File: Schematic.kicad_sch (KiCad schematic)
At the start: 51 parts, among them IC601 AZV3002S-13, J101 KLDX-0202-B, J102 EBWA-02-B, J103 EBWA-02-B, J104 KLDX-0202-B, Q201 MCU18P10Y-TP, Q501 BC846, Q502 MCU18P10Y-TP, U401 LM4040DBZ-5

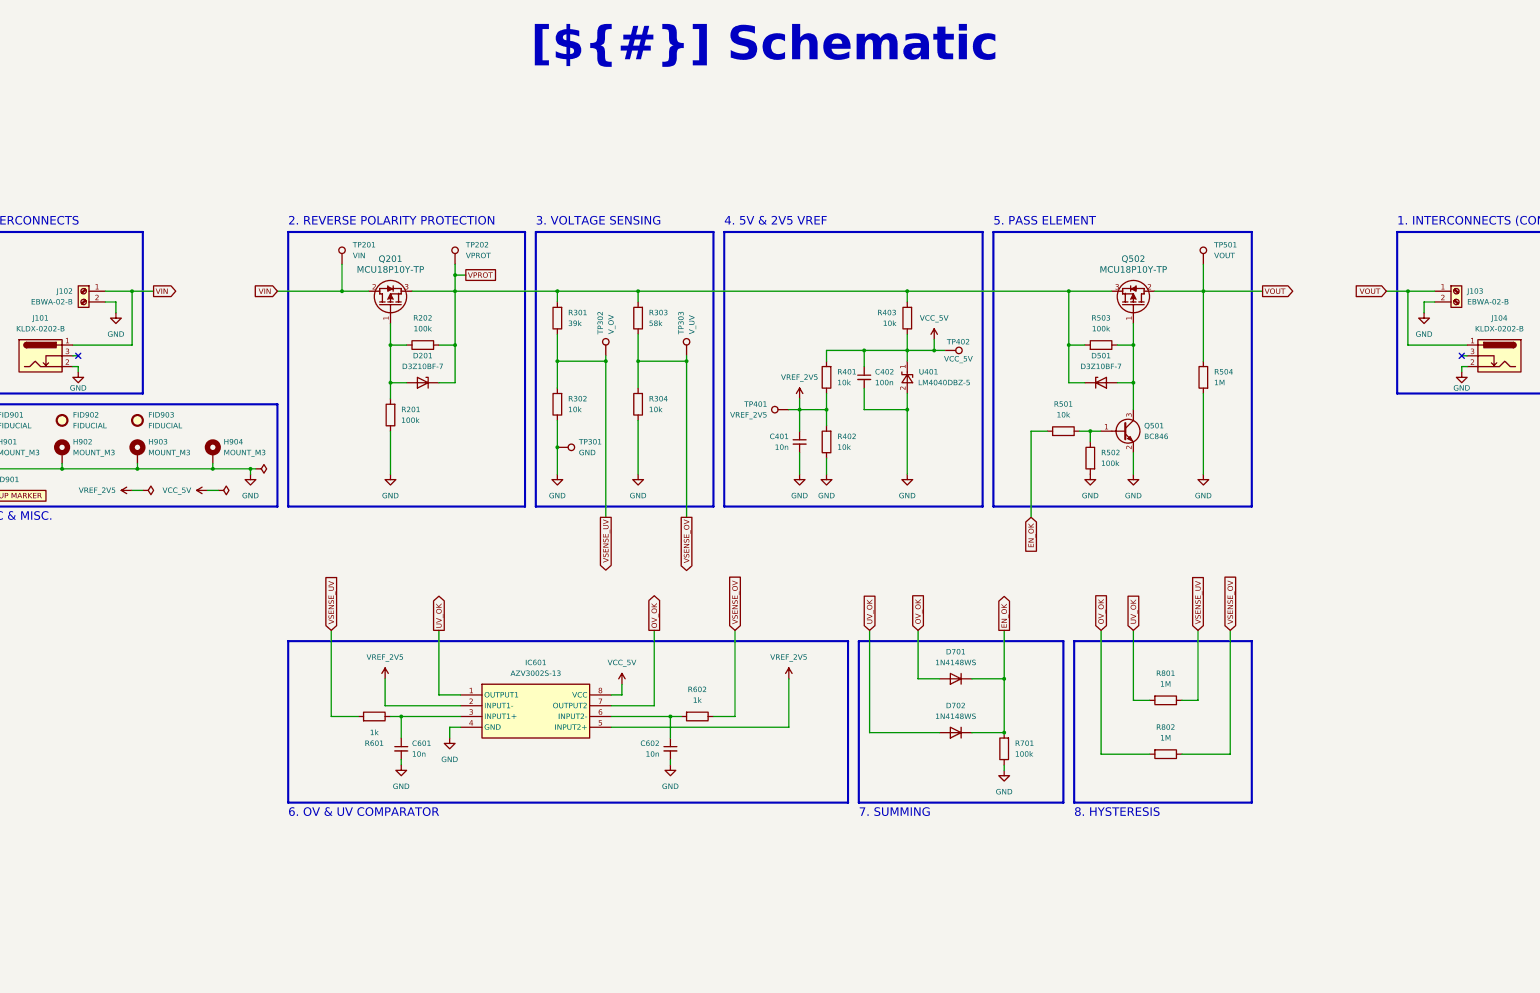
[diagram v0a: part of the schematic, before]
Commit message: fix: fix properties of actives with MPN
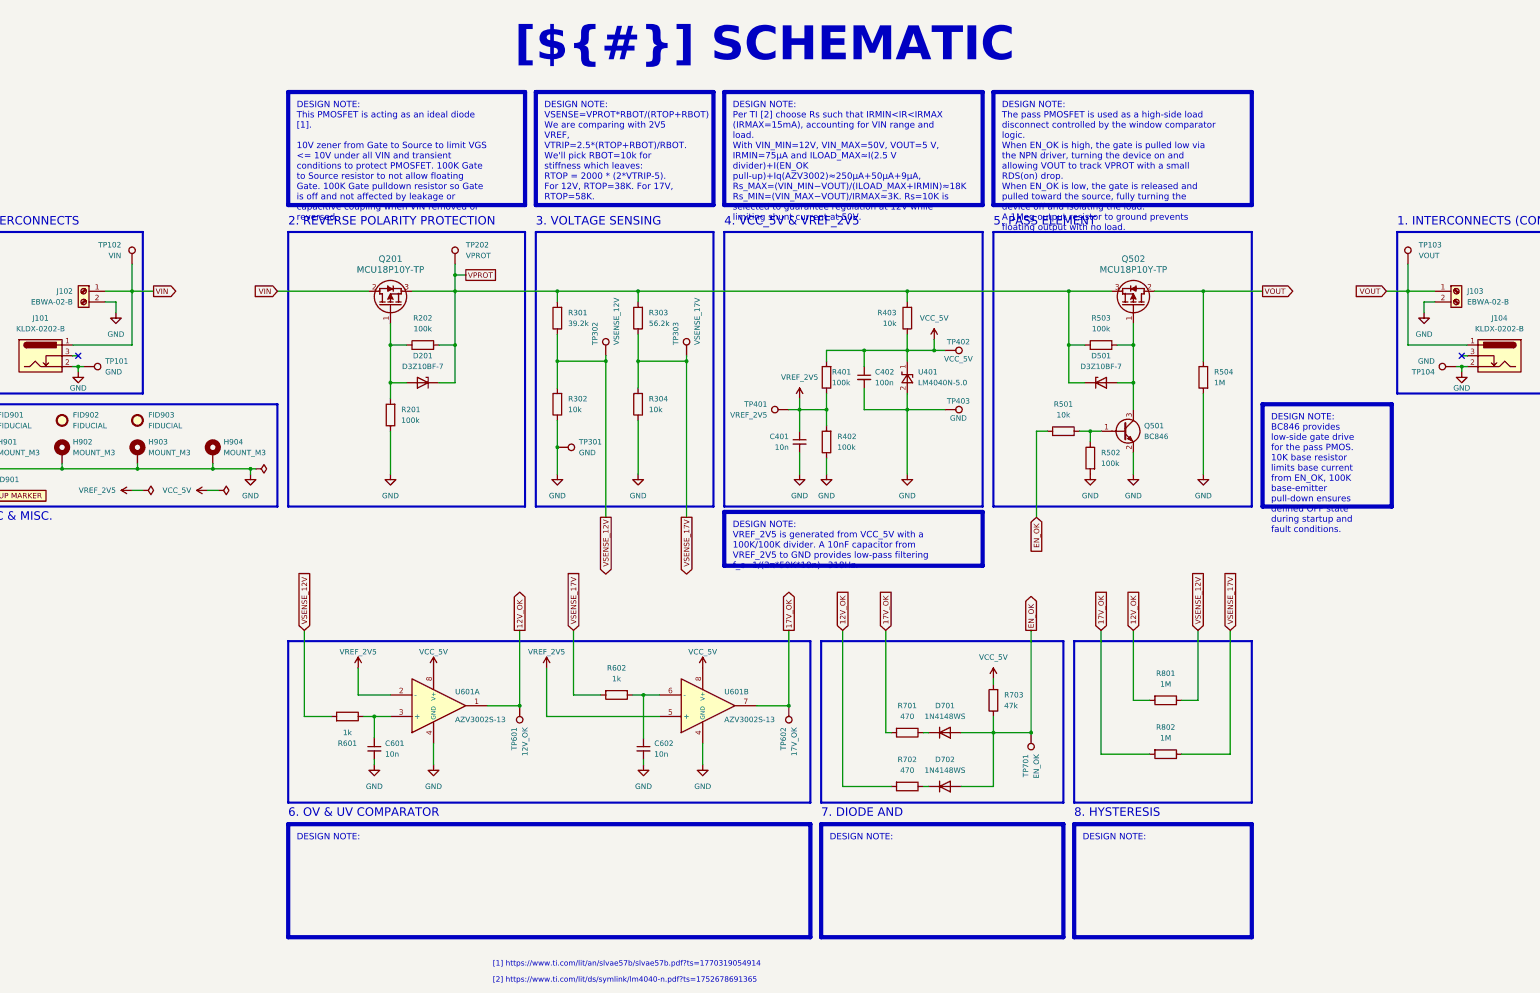
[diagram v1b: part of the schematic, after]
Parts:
- removed IC601: AZV3002S-13, Package_SO:Diodes_SO-8EP, symbol AZV3002S-13:AZV3002S-13
- added R701, R702: 470, Resistor_SMD:R_1206_3216Metric_Pad1.30x1.75mm_HandSolder, symbol Device:R
- added TP101, TP104, TP403: GND, TestPoint:TestPoint_Pad_D1.5mm, symbol Connector:TestPoint
- added TP601: 12V_OK, TestPoint:TestPoint_Pad_D1.5mm, symbol Connector:TestPoint
- added TP602: 17V_OK, TestPoint:TestPoint_Pad_D1.5mm, symbol Connector:TestPoint
- added TP701: EN_OK, TestPoint:TestPoint_Pad_D1.5mm, symbol Connector:TestPoint
- added U601: AZV3002S-13, Package_SO:Diodes_SO-8EP, symbol AZV3002S-13:AZV3002S-13
- C401, C601, C602: footprint (none) -> Capacitor_SMD:C_0603_1608Metric_Pad1.08x0.95mm_HandSolder; Dielectric (none) -> X7R; MPN (none) -> C1608X7R1H103KT; Manufacturer (none) -> TPK; Tolerance (none) -> 10%; Voltage_Rating (none) -> 50V
- C402: footprint (none) -> Capacitor_SMD:C_0603_1608Metric_Pad1.08x0.95mm_HandSolder; Dielectric (none) -> X7R; MPN (none) -> C1608X7R1C104KT; Manufacturer (none) -> TPK; Tolerance (none) -> 10%; Voltage_Rating (none) -> 16V
- D201, D501: MPN (none) -> D3Z10BF-7; Manufacturer (none) -> Diodes Incorporated
- D701, D702: MPN (none) -> 1N4148WS; Manufacturer (none) -> Diotec Semiconductor
- FID901, FID902, FID903: footprint (none) -> Fiducial:Fiducial_Cross_0.5mm_Mask2mm
- H901, H902, H903, H904: footprint (none) -> MountingHole:MountingHole_3.2mm_M3_ISO7380_Pad
- J101: MPN (none) -> KLDX-0202-B; Manufacturer (none) -> Kycon Inc
- J102: MPN (none) -> EBWA-02-B; Manufacturer (none) -> Adam Tech
- Q201, Q502: MPN (none) -> MCU18P10Y-TP; Manufacturer (none) -> MCC (Micro Commercial Components)
- Q501: MPN (none) -> BC846; Manufacturer (none) -> Nexperia USA Inc.
- R301: value 39k -> 39.2k
- R303: value 58k -> 56.2k
- R401, R402: value 10k -> 100k
- R703: renamed from R701; value 100k -> 47k
- TP102: renamed from TP201; footprint TestPoint:TestPoint_Pad_D2.5mm -> TestPoint:TestPoint_Pad_D1.5mm; now left out of the parts list
- TP103: renamed from TP501; footprint TestPoint:TestPoint_Pad_D2.5mm -> TestPoint:TestPoint_Pad_D1.5mm; now left out of the parts list
- TP202, TP401, TP402: footprint TestPoint:TestPoint_Pad_D2.5mm -> TestPoint:TestPoint_Pad_D1.5mm; now left out of the parts list
- TP301: footprint TestPoint:TestPoint_Pad_D2.5mm -> TestPoint:TestPoint_Pad_D1.5mm
- TP302: value V_OV -> VSENSE_12V; footprint TestPoint:TestPoint_Pad_D2.5mm -> TestPoint:TestPoint_Pad_D1.5mm; now left out of the parts list
- TP303: value V_UV -> VSENSE_17V; footprint TestPoint:TestPoint_Pad_D2.5mm -> TestPoint:TestPoint_Pad_D1.5mm; now left out of the parts list
- U401: value LM4040DBZ-5 -> LM4040N-5.0; MPN (none) -> LM4040CIM3-5.0/NOPB; Manufacturer (none) -> Texas Instruments
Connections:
- net EN_OK: now also D701.2 (A), D702.2 (A), R703.1, TP701.1; no longer D701.1 (K), D702.1 (K), R703.2
- net GND: now also TP101.1, TP104.1, TP403.1, U601.4 (GND), U601.4 (GND); no longer R703.1
- net VCC_5V: now also R703.2, U601.8 (V+), U601.8 (V+)
- net VREF_2V5: now also U601.2 (-), U601.5 (+)
- net at C601.1, R601.1: now also U601.3 (+)
- net at C602.1: now also R602.1, U601.6 (-); no longer R602.2
- net OV_OK renamed 17V_OK
- net 17V_OK: now also R701.2, TP602.1, U601.7; no longer D701.2 (A)
- net UV_OK renamed 12V_OK
- net 12V_OK: now also R702.2, TP601.1, U601.1; no longer D702.2 (A)
- net VSENSE_OV renamed VSENSE_17V
- net VSENSE_17V: now also R602.2; no longer R602.1
- net VSENSE_UV renamed VSENSE_12V
- new net: D702.1 (K), R702.1
- new net: D701.1 (K), R701.1
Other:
- note added: "4. VCC_5V & VREF_2V5"
- note added: "7. DIODE AND"
- note added: "[1] https://www.ti.com/lit/an/slvae57b/slvae57b.pdf?ts=1770319054914"
- note added: "[2] https://www.ti.com/lit/ds/symlink/lm4040-n.pdf?ts=1752678691365"
- note removed: "4. 5V & 2V5 VREF"
- note removed: "7. SUMMING"
- title: Schematic -> SCHEMATIC
- moved on the sheet: D701, D702, R601, R703, TP102, TP103

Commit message: fix: template changes
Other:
- moved on the sheet: C401, C402, C601, C602, D201, D501, D701, D702, FID901, FID902, FID903, H901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
